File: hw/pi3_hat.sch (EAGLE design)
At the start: 109 parts, among them J1 XT30P, J2 XT30P, U1 AP64351SO8EP, U10 CAT24C32SOIC8, U11 STM32G474CEU6, U12 TCAN334GSOT23, U13 TCAN334GSOT23, U2 DMMT5401, U3 DMG2305UX, U4 STM32G474CEU6, U5 TCAN334GSOT23, U6 TCAN334GSOT23, U7 STM32G474CEU6, U8 BMI088LGA16, U9 TCAN334GSOT23

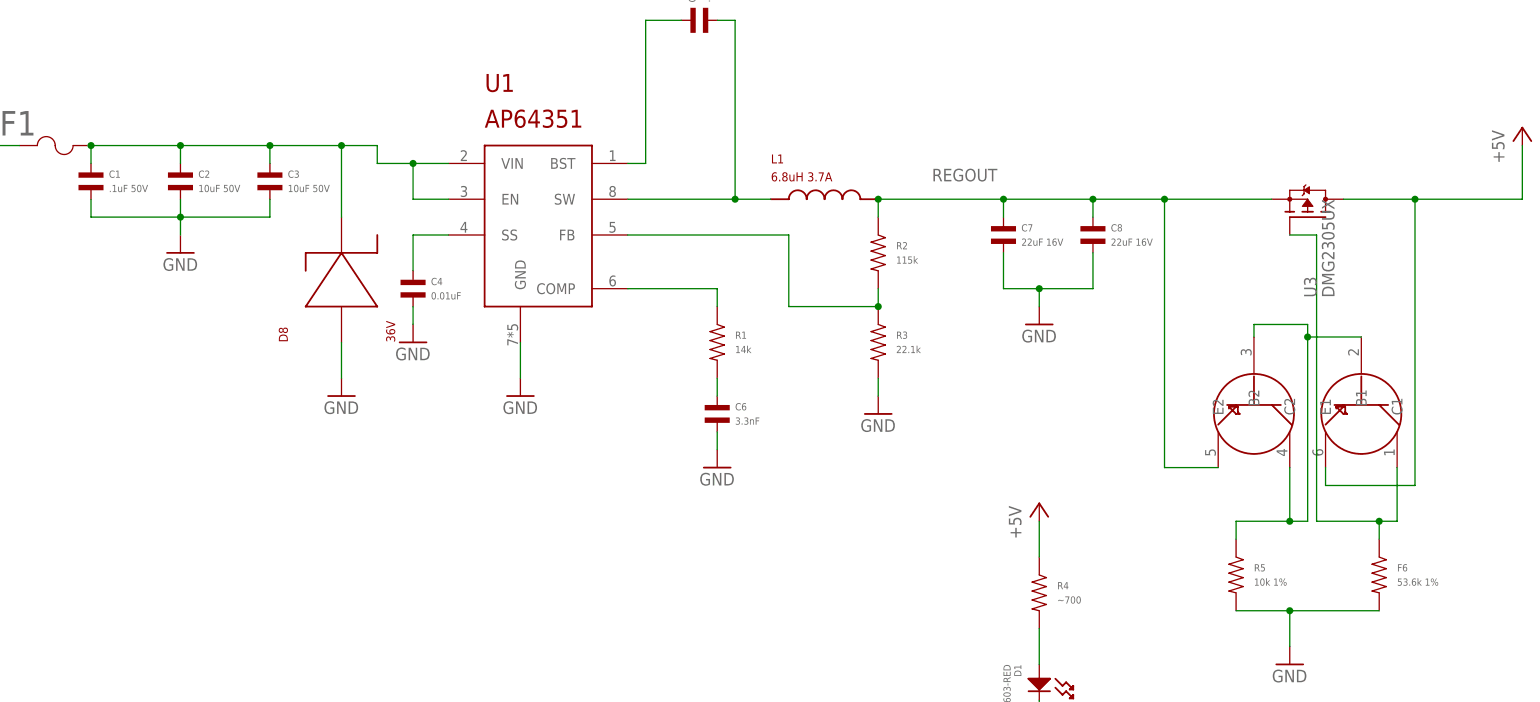
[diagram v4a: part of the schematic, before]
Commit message: Route power input
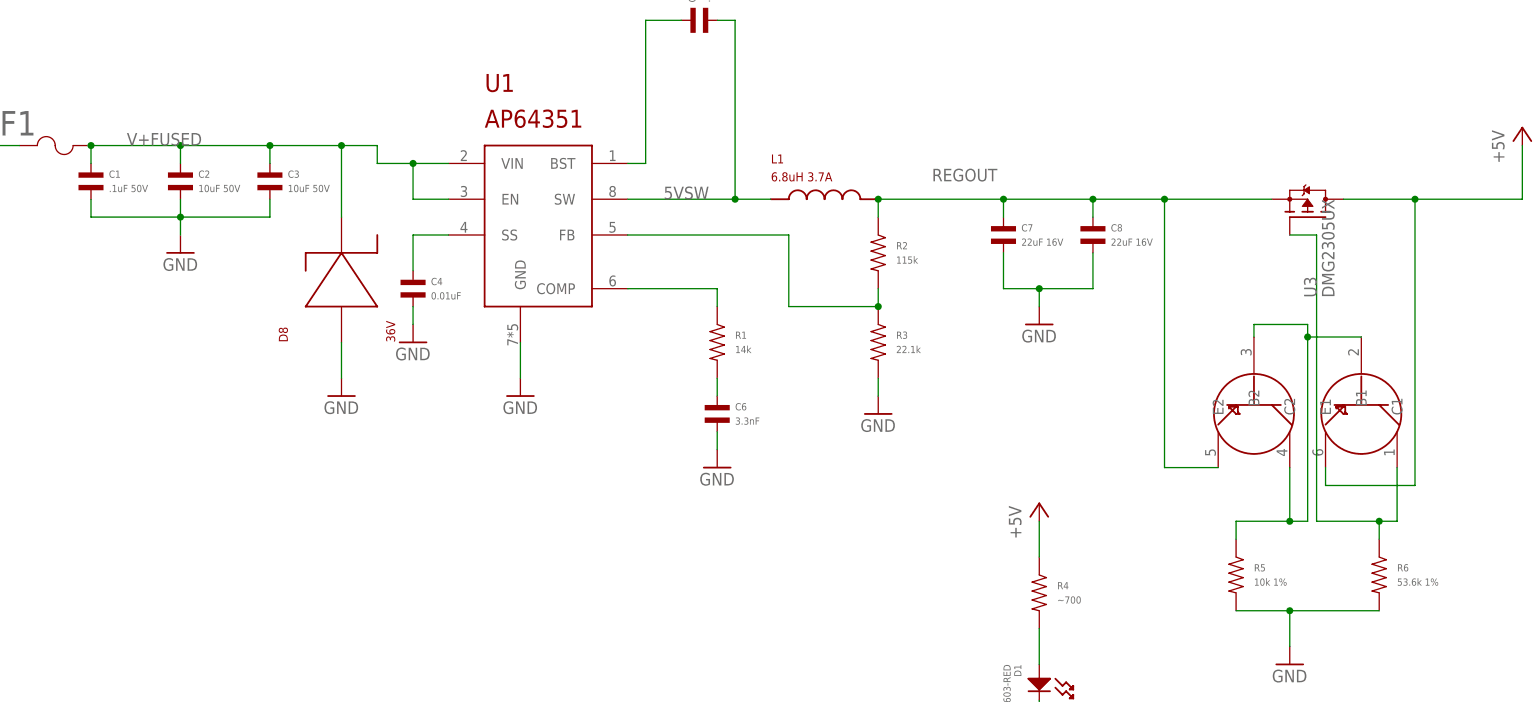
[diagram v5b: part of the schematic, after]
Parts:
- renumbered F6 to R6
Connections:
- net N$10 renamed V+FUSED
- net N$20 renamed 5VSW
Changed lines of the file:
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@@
 <attribute name="MPN" value="ERJ-3EKF1002V"/>
 </part>
-<part name="F6" library="mfpassives" deviceset="RESISTOR" device="_0603" value="53.6k 1%">
+<part name="R6" library="mfpassives" deviceset="RESISTOR" device="_0603" value="53.6k 1%">
 <attribute name="MF" value="Panasonic"/>
 <attribute name="MPN" value="ERJ-3EKF5362V"/>
@@
 <attribute name="MF" x="170.18" y="223.52" size="1.778" layer="96" display="off"/>
 </instance>
-<instance part="F6" gate="G$1" x="190.5" y="223.52">
+<instance part="R6" gate="G$1" x="190.5" y="223.52">
 <attribute name="MF" x="190.5" y="223.52" size="1.778" layer="96" display="off"/>
 </instance>
@@
 <junction x="177.8" y="218.44"/>
 <pinref part="R5" gate="G$1" pin="P$2"/>
-<pinref part="F6" gate="G$1" pin="P$2"/>
+<pinref part="R6" gate="G$1" pin="P$2"/>
 </segment>
 <segment>
@@
 <wire x1="193.04" y1="231.14" x2="193.04" y2="238.76" width="0.1524" layer="91"/>
 <junction x="190.5" y="231.14"/>
-<pinref part="F6" gate="G$1" pin="P$1"/>
+<pinref part="R6" gate="G$1" pin="P$1"/>
 </segment>
 </net>
@@
 </segment>
 </net>
-<net name="N$10" class="0">
+<net name="V+FUSED" class="0">
 <segment>
 <pinref part="F1" gate="A" pin="2"/>
@@
 <wire x1="43.18" y1="274.32" x2="43.18" y2="284.48" width="0.1524" layer="91"/>
 <junction x="43.18" y="284.48"/>
+<label x="12.7" y="284.48" size="1.778" layer="95"/>
 </segment>
 </net>
@@
 </segment>
 </net>
-<net name="N$20" class="0">
+<net name="5VSW" class="0">
 <segment>
 <pinref part="C5" gate="G$1" pin="P$2"/>
@@
 <wire x1="99.06" y1="276.86" x2="104.14" y2="276.86" width="0.1524" layer="91"/>
 <junction x="99.06" y="276.86"/>
+<label x="88.9" y="276.86" size="1.778" layer="95"/>
 </segment>
 </net>

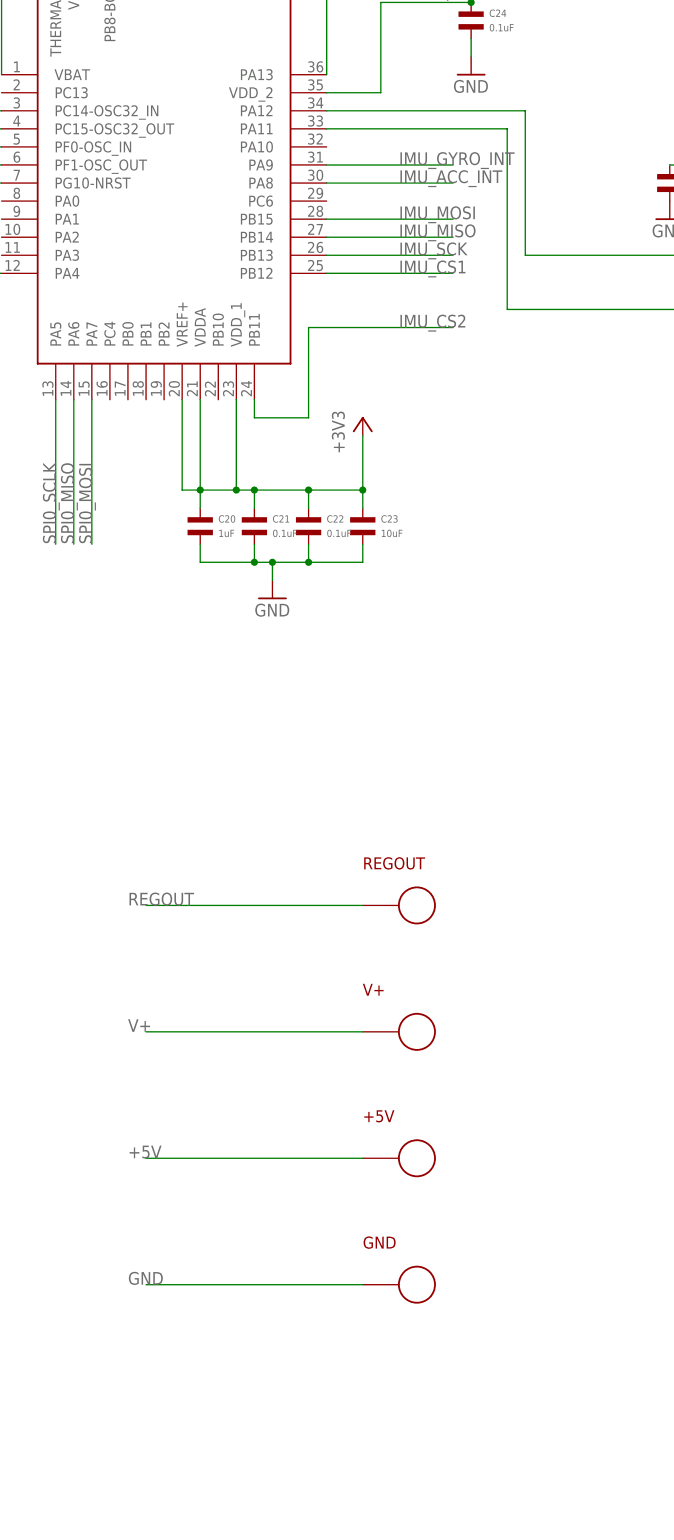
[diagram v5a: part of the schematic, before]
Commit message: More fiddling, and add a 3.3v test point
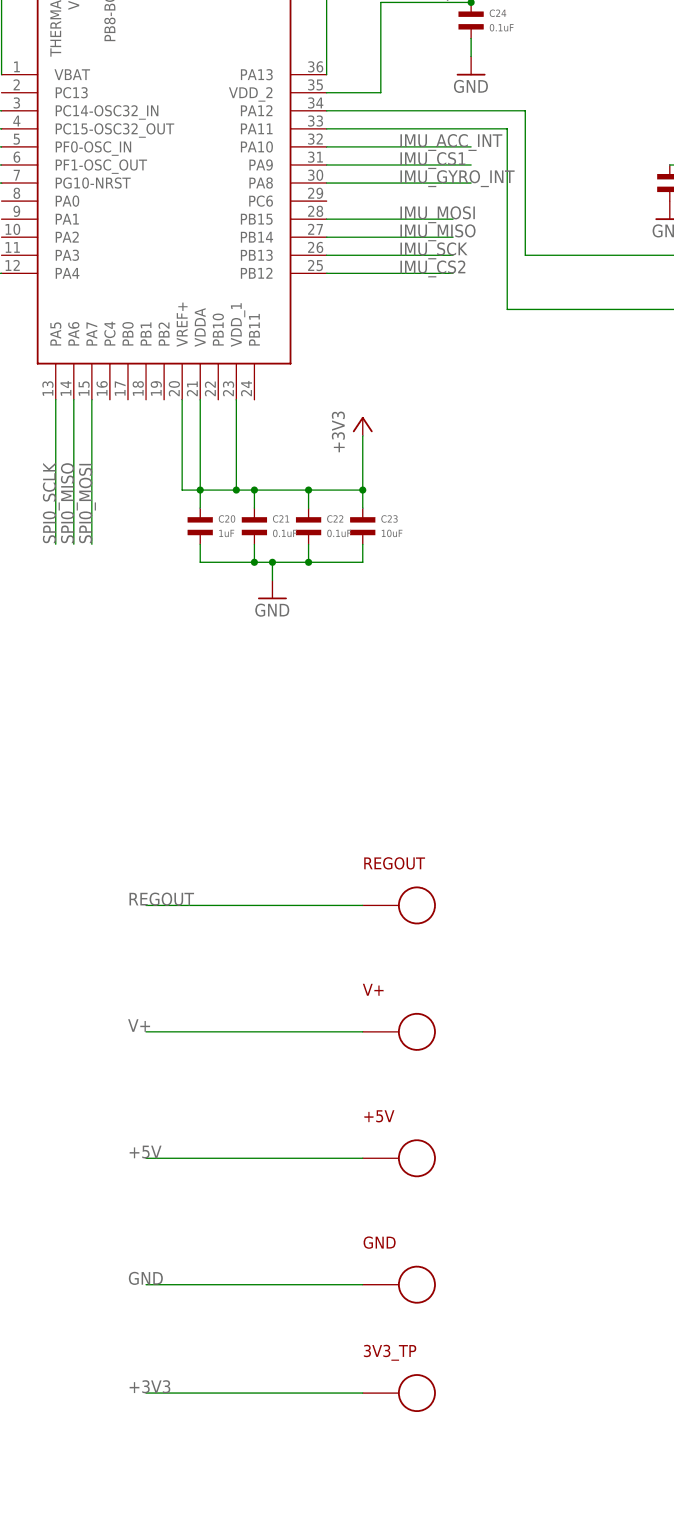
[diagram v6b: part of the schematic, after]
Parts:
- added 3V3_TP: PAD24AWG_PAD, pi3_hat:PAD24AWG_PAD
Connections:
- net +3V3: now also 3V3_TP.P$1
- net IMU_ACC_INT: now also U7.PA10; no longer U7.PA8
- net IMU_CS1: now also U7.PA9; no longer U7.PB12
- net IMU_CS2: now also U7.PB12; no longer U7.PB11
- net IMU_GYRO_INT: now also U7.PA8; no longer U7.PA9
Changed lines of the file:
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@@
 </part>
 <part name="GND57" library="supply1" deviceset="GND" device=""/>
+<part name="3V3_TP" library="pi3_hat" deviceset="PAD" device="24AWG_PAD"/>
 </parts>
 <sheets>
@@
 </instance>
 <instance part="GND57" gate="1" x="43.18" y="248.92"/>
+<instance part="3V3_TP" gate="G$1" x="728.98" y="66.04"/>
 </instances>
 <busses>
@@
 <wire x1="355.6" y1="71.12" x2="355.6" y2="83.82" width="0.1524" layer="91"/>
 </segment>
+<segment>
+<pinref part="3V3_TP" gate="G$1" pin="P$1"/>
+<wire x1="721.36" y1="66.04" x2="690.88" y2="66.04" width="0.1524" layer="91"/>
+<label x="688.34" y="66.04" size="1.778" layer="95"/>
+</segment>
 </net>
 <net name="PI_TX_3V" class="0">
@@
 </segment>
 <segment>
+<pinref part="U7" gate="G$1" pin="PA9"/>
+<wire x1="716.28" y1="238.76" x2="736.6" y2="238.76" width="0.1524" layer="91"/>
+<label x="726.44" y="238.76" size="1.778" layer="95"/>
+</segment>
+</net>
+<net name="IMU_CS2" class="0">
+<segment>
+<pinref part="U8" gate="G$1" pin="CSB2"/>
+<wire x1="787.4" y1="281.94" x2="764.54" y2="281.94" width="0.1524" layer="91"/>
+<label x="764.54" y="281.94" size="1.778" layer="95" font="vector"/>
+</segment>
+<segment>
 <pinref part="U7" gate="G$1" pin="PB12"/>
 <wire x1="716.28" y1="223.52" x2="734.06" y2="223.52" width="0.1524" layer="91"/>
@@
 </segment>
 </net>
-<net name="IMU_CS2" class="0">
-<segment>
-<pinref part="U8" gate="G$1" pin="CSB2"/>
-<wire x1="787.4" y1="281.94" x2="764.54" y2="281.94" width="0.1524" layer="91"/>
-<label x="764.54" y="281.94" size="1.778" layer="95" font="vector"/>
-</segment>
-<segment>
-<pinref part="U7" gate="G$1" pin="PB11"/>
-<wire x1="706.12" y1="205.74" x2="706.12" y2="203.2" width="0.1524" layer="91"/>
-<wire x1="706.12" y1="203.2" x2="713.74" y2="203.2" width="0.1524" layer="91"/>
-<wire x1="713.74" y1="203.2" x2="713.74" y2="215.9" width="0.1524" layer="91"/>
-<wire x1="713.74" y1="215.9" x2="734.06" y2="215.9" width="0.1524" layer="91"/>
-<label x="726.44" y="215.9" size="1.778" layer="95"/>
-</segment>
-</net>
 <net name="IMU_ACC_INT" class="0">
 <segment>
@@
 </segment>
 <segment>
-<pinref part="U7" gate="G$1" pin="PA8"/>
-<wire x1="716.28" y1="236.22" x2="734.06" y2="236.22" width="0.1524" layer="91"/>
-<label x="726.44" y="236.22" size="1.778" layer="95" font="vector"/>
+<pinref part="U7" gate="G$1" pin="PA10"/>
+<wire x1="716.28" y1="241.3" x2="736.6" y2="241.3" width="0.1524" layer="91"/>
+<label x="726.44" y="241.3" size="1.778" layer="95"/>
 </segment>
 </net>
@@
 </segment>
 <segment>
-<pinref part="U7" gate="G$1" pin="PA9"/>
-<wire x1="716.28" y1="238.76" x2="734.06" y2="238.76" width="0.1524" layer="91"/>
-<label x="726.44" y="238.76" size="1.778" layer="95" font="vector"/>
-</segment>
-</net>
+<pinref part="U7" gate="G$1" pin="PA8"/>
+<wire x1="716.28" y1="236.22" x2="736.6" y2="236.22" width="0.1524" layer="91"/>
+<label x="726.44" y="236.22" size="1.778" layer="95"/>
+</segment>
+</net>

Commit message: Select parts
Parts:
- +5V, 3V3_TP, GND, J1, J2, REGOUT, SPI0_CS0, SPI0_MISO, SPI0_MOSI, SPI0_SCLK, SPI1_CS0, SPI1_CS1, SPI1_MISO, SPI1_MOSI, SPI1_SCLK, V+: POPULATE (none) -> 0
- C6: value 3.3nF -> 4.7nF; HOUSEPART (none) -> YES; MPN (none) -> MF-CAP-0402-4.7nF
- D3, D5, D7: MPN (none) -> MF-LED-0603-GREEN
- F1: MF (none) -> VISHAY
- J3: MF (none) -> Wurth Elektornik; MPN (none) -> 61300821121; POPULATE (none) -> 1
- J4: MF (none) -> Sullins; MPN (none) -> PPPC202LFBN-RC; POPULATE (none) -> 0
- JC1, JC2, JC3, JC4, JC5: MF (none) -> JST; MPN (none) -> B3B-PH-SM4-TB(LF)(SN); POPULATE (none) -> 1
- JD1, JD2, JD3: MF (none) -> JST; MPN (none) -> B6B-ZR-SM4-TF(LF)(SN); POPULATE (none) -> 1
- JP1: HOUSEPART (none) -> YES; MPN (none) -> MF-CON-2.54mm-01x02; POPULATE (none) -> 1
- R1: value 14k -> 15k; HOUSEPART (none) -> YES; MPN (none) -> MF-RES-0402-15K
- R10, R13, R19, R20, R9: HOUSEPART (none) -> YES; MPN (none) -> MF-RES-0402-100
- R11, R12, R17, R18, R7, R8: HOUSEPART (none) -> YES; MPN (none) -> MF-RES-0402-220
- R14: HOUSEPART (none) -> YES; MPN (none) -> MF-RES-0402-1K
- R15, R16: value 3.9k 1% -> 4.7k; HOUSEPART (none) -> YES; MPN (none) -> MF-RES-0402-4.7K
- R2: MF (none) -> YAGEO; MPN (none) -> RC0402FR-07115KL
- R3: MF (none) -> YAGEO; MPN (none) -> RC0402FR-0722K1L
- R4: value ~700 -> 560; HOUSEPART (none) -> YES; MPN (none) -> MF-RES-0402-560
- R5: MF Panasonic -> YAGEO; MPN ERJ-3EKF1002V -> RC0402FR-0710KL
- R6: MF Panasonic -> YAGEO; MPN ERJ-3EKF5362V -> RC0402FR-0753K6L
- U11, U4, U7: MF (none) -> ST; MPN (none) -> STM32G474CEU6; POPULATE (none) -> 1
- U12, U13, U5, U6, U9: MF (none) -> TI; MPN (none) -> TCAN334GDCNT; POPULATE (none) -> 1
- U8: MF (none) -> BOSCH; MPN (none) -> BMI088; POPULATE (none) -> 1
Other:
- note added: "mjbots quad pi3 hat r4 (c) jjp@pobox.com 2020 Licensed under the Apache 2.0 License"
- note removed: "mjmech pi3 hat r4 (c) jjp@pobox.com 2020 Licensed under the Apache 2.0 License"

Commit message: Minor silk tweaks, re-autoroute with bottom layer up/down
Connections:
- new net PI_RX_3V: J4.10
- net N$32: now also JD2.2; no longer JD3.2
- net N$33: now also JD2.3; no longer JD3.3
- net N$34: now also JD2.5; no longer JD3.5
- net N$47: now also JD3.2; no longer JD2.2
- net N$48: now also JD3.3; no longer JD2.3
- net N$49: now also JD3.5; no longer JD2.5
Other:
- moved on the sheet: JD2, JD3
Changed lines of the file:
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@@
 </part>
 <part name="GND27" library="supply1" deviceset="GND" device=""/>
-<part name="JD3" library="pi3_hat" deviceset="JST-ZH6" device="SMT_VERT">
+<part name="JD2" library="pi3_hat" deviceset="JST-ZH6" device="SMT_VERT">
 <attribute name="MF" value="JST"/>
 <attribute name="MPN" value="B6B-ZR-SM4-TF(LF)(SN)"/>
@@
 </part>
 <part name="GND40" library="supply1" deviceset="GND" device=""/>
-<part name="JD2" library="pi3_hat" deviceset="JST-ZH6" device="SMT_VERT">
+<part name="JD3" library="pi3_hat" deviceset="JST-ZH6" device="SMT_VERT">
 <attribute name="MF" value="JST"/>
 <attribute name="MPN" value="B6B-ZR-SM4-TF(LF)(SN)"/>
@@
 <instance part="C34" gate="G$1" x="383.54" y="7.62"/>
 <instance part="GND27" gate="1" x="337.82" y="45.72"/>
-<instance part="JD3" gate="A" x="294.64" y="121.92">
+<instance part="JD2" gate="A" x="294.64" y="121.92">
 <attribute name="POPULATE" x="294.64" y="121.92" size="1.778" layer="96" display="off"/>
 <attribute name="MPN" x="294.64" y="121.92" size="1.778" layer="96" display="off"/>
@@
 <instance part="C20" gate="G$1" x="698.5" y="187.96"/>
 <instance part="GND40" gate="1" x="652.78" y="226.06"/>
-<instance part="JD2" gate="A" x="609.6" y="302.26">
+<instance part="JD3" gate="A" x="609.6" y="302.26">
 <attribute name="POPULATE" x="609.6" y="302.26" size="1.778" layer="96" display="off"/>
 <attribute name="MPN" x="609.6" y="302.26" size="1.778" layer="96" display="off"/>
@@
 </segment>
 <segment>
-<pinref part="JD3" gate="A" pin="4"/>
+<pinref part="JD2" gate="A" pin="4"/>
 <pinref part="GND28" gate="1" pin="GND"/>
 <wire x1="299.72" y1="121.92" x2="317.5" y2="121.92" width="0.1524" layer="91"/>
@@
 </segment>
 <segment>
-<pinref part="JD2" gate="A" pin="4"/>
+<pinref part="JD3" gate="A" pin="4"/>
 <pinref part="GND41" gate="1" pin="GND"/>
 <wire x1="614.68" y1="302.26" x2="632.46" y2="302.26" width="0.1524" layer="91"/>
@@
 </segment>
 <segment>
-<pinref part="JD3" gate="A" pin="6"/>
+<pinref part="JD2" gate="A" pin="6"/>
 <pinref part="+3V10" gate="G$1" pin="+3V3"/>
 <wire x1="299.72" y1="116.84" x2="307.34" y2="116.84" width="0.1524" layer="91"/>
@@
 </segment>
 <segment>
-<pinref part="JD2" gate="A" pin="6"/>
+<pinref part="JD3" gate="A" pin="6"/>
 <pinref part="+3V17" gate="G$1" pin="+3V3"/>
 <wire x1="614.68" y1="297.18" x2="622.3" y2="297.18" width="0.1524" layer="91"/>
@@
 <net name="PI_RX_3V" class="0">
 <segment>
-<wire x1="63.5" y1="111.76" x2="83.82" y2="111.76" width="0.1524" layer="91"/>
+<wire x1="60.96" y1="111.76" x2="83.82" y2="111.76" width="0.1524" layer="91"/>
 <label x="78.74" y="111.76" size="1.778" layer="95" font="vector"/>
+<pinref part="J4" gate="A" pin="10"/>
 </segment>
 </net>
@@
 <net name="N$32" class="0">
 <segment>
-<pinref part="JD3" gate="A" pin="2"/>
+<pinref part="JD2" gate="A" pin="2"/>
 <wire x1="299.72" y1="127" x2="337.82" y2="127" width="0.1524" layer="91"/>
 <pinref part="C32" gate="G$1" pin="P$1"/>
@@
 <net name="N$33" class="0">
 <segment>
-<pinref part="JD3" gate="A" pin="3"/>
+<pinref part="JD2" gate="A" pin="3"/>
 <wire x1="299.72" y1="124.46" x2="406.4" y2="124.46" width="0.1524" layer="91"/>
 <pinref part="U11" gate="G$1" pin="PA13"/>
@@
 <net name="N$34" class="0">
 <segment>
-<pinref part="JD3" gate="A" pin="5"/>
+<pinref part="JD2" gate="A" pin="5"/>
 <wire x1="299.72" y1="119.38" x2="393.7" y2="119.38" width="0.1524" layer="91"/>
 <pinref part="U11" gate="G$1" pin="PA14"/>
@@
 <net name="N$47" class="0">
 <segment>
-<pinref part="JD2" gate="A" pin="2"/>
+<pinref part="JD3" gate="A" pin="2"/>
 <wire x1="614.68" y1="307.34" x2="652.78" y2="307.34" width="0.1524" layer="91"/>
 <pinref part="C18" gate="G$1" pin="P$1"/>
@@
 <net name="N$48" class="0">
 <segment>
-<pinref part="JD2" gate="A" pin="3"/>
+<pinref part="JD3" gate="A" pin="3"/>
 <wire x1="614.68" y1="304.8" x2="716.28" y2="304.8" width="0.1524" layer="91"/>
 <pinref part="U7" gate="G$1" pin="PA13"/>
@@
 <net name="N$49" class="0">
 <segment>
-<pinref part="JD2" gate="A" pin="5"/>
+<pinref part="JD3" gate="A" pin="5"/>
 <wire x1="614.68" y1="299.72" x2="708.66" y2="299.72" width="0.1524" layer="91"/>
 <pinref part="U7" gate="G$1" pin="PA14"/>
